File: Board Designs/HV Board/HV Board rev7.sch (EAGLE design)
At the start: 58 parts, among them IC1 OKI-78SR, IC2 NE5532SOIC

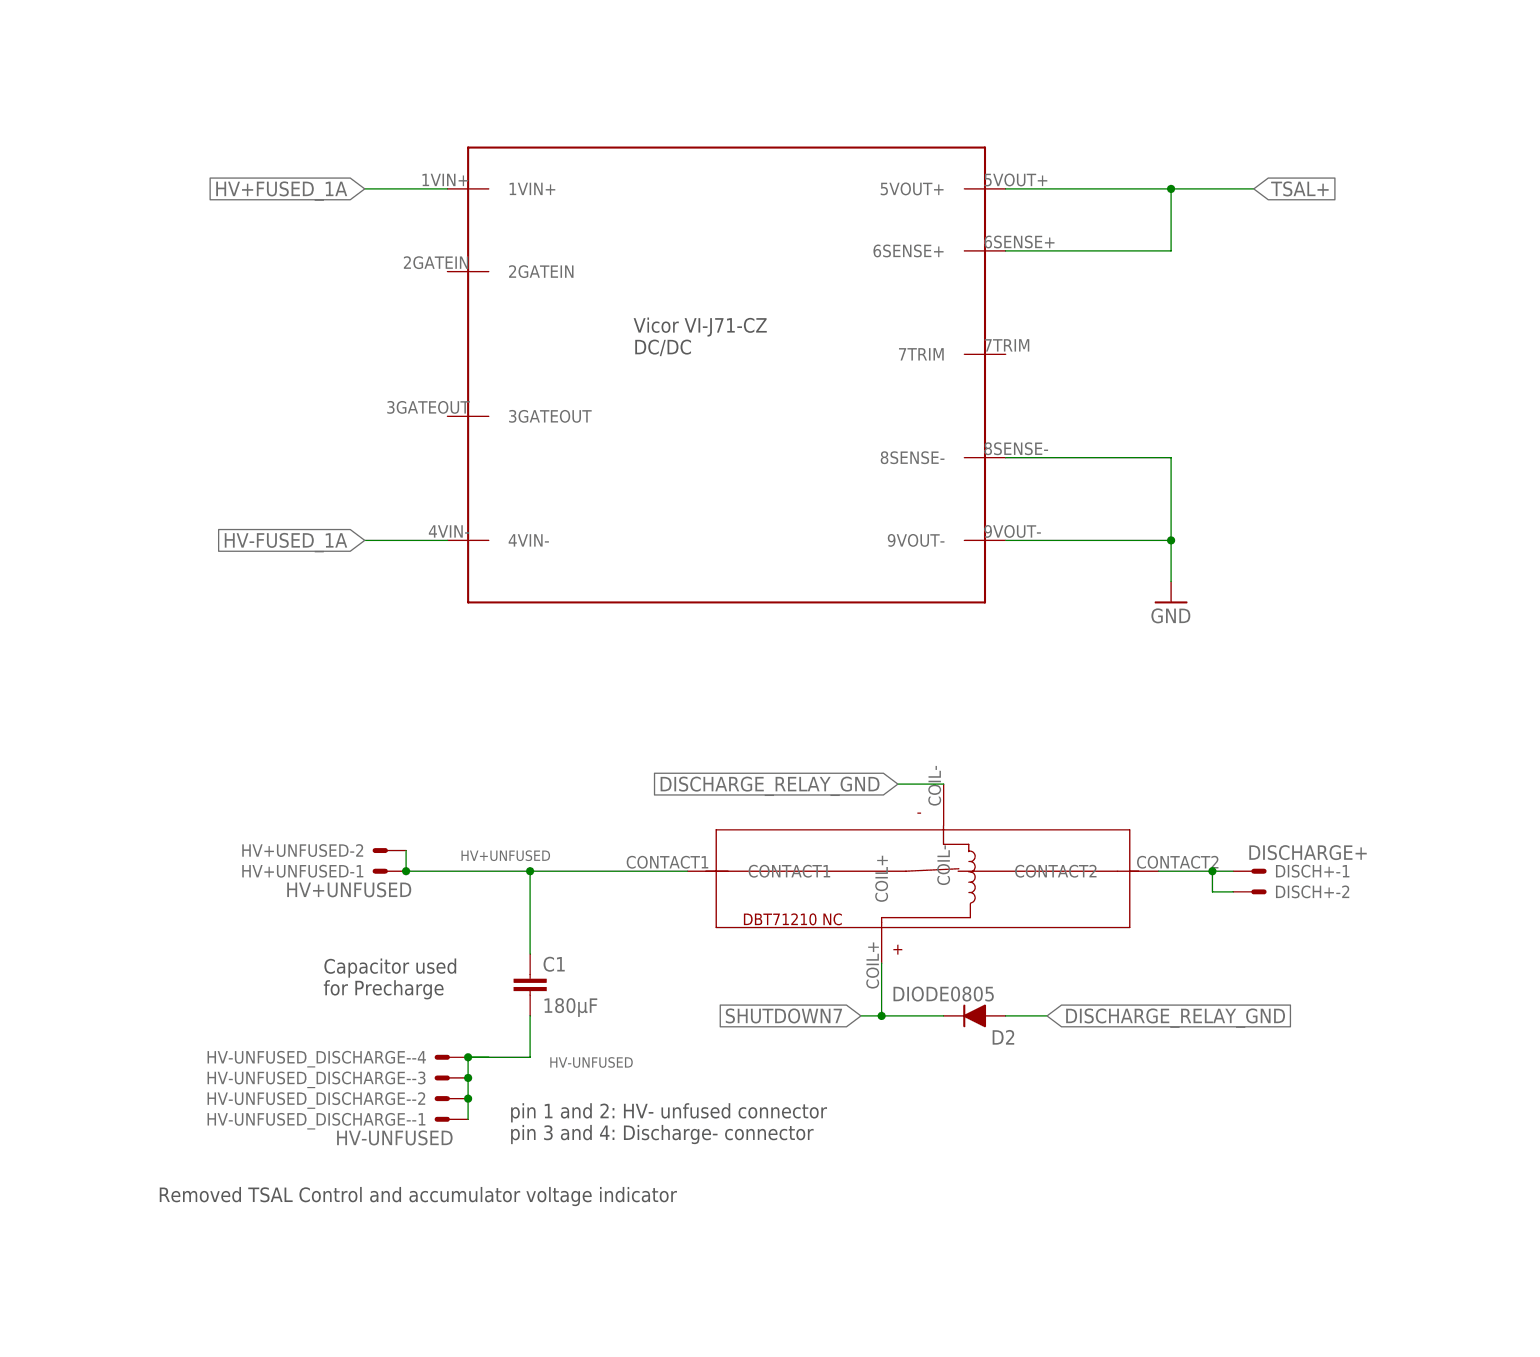
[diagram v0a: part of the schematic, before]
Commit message: Updated cynergy relay in lib, fixed DRC issues
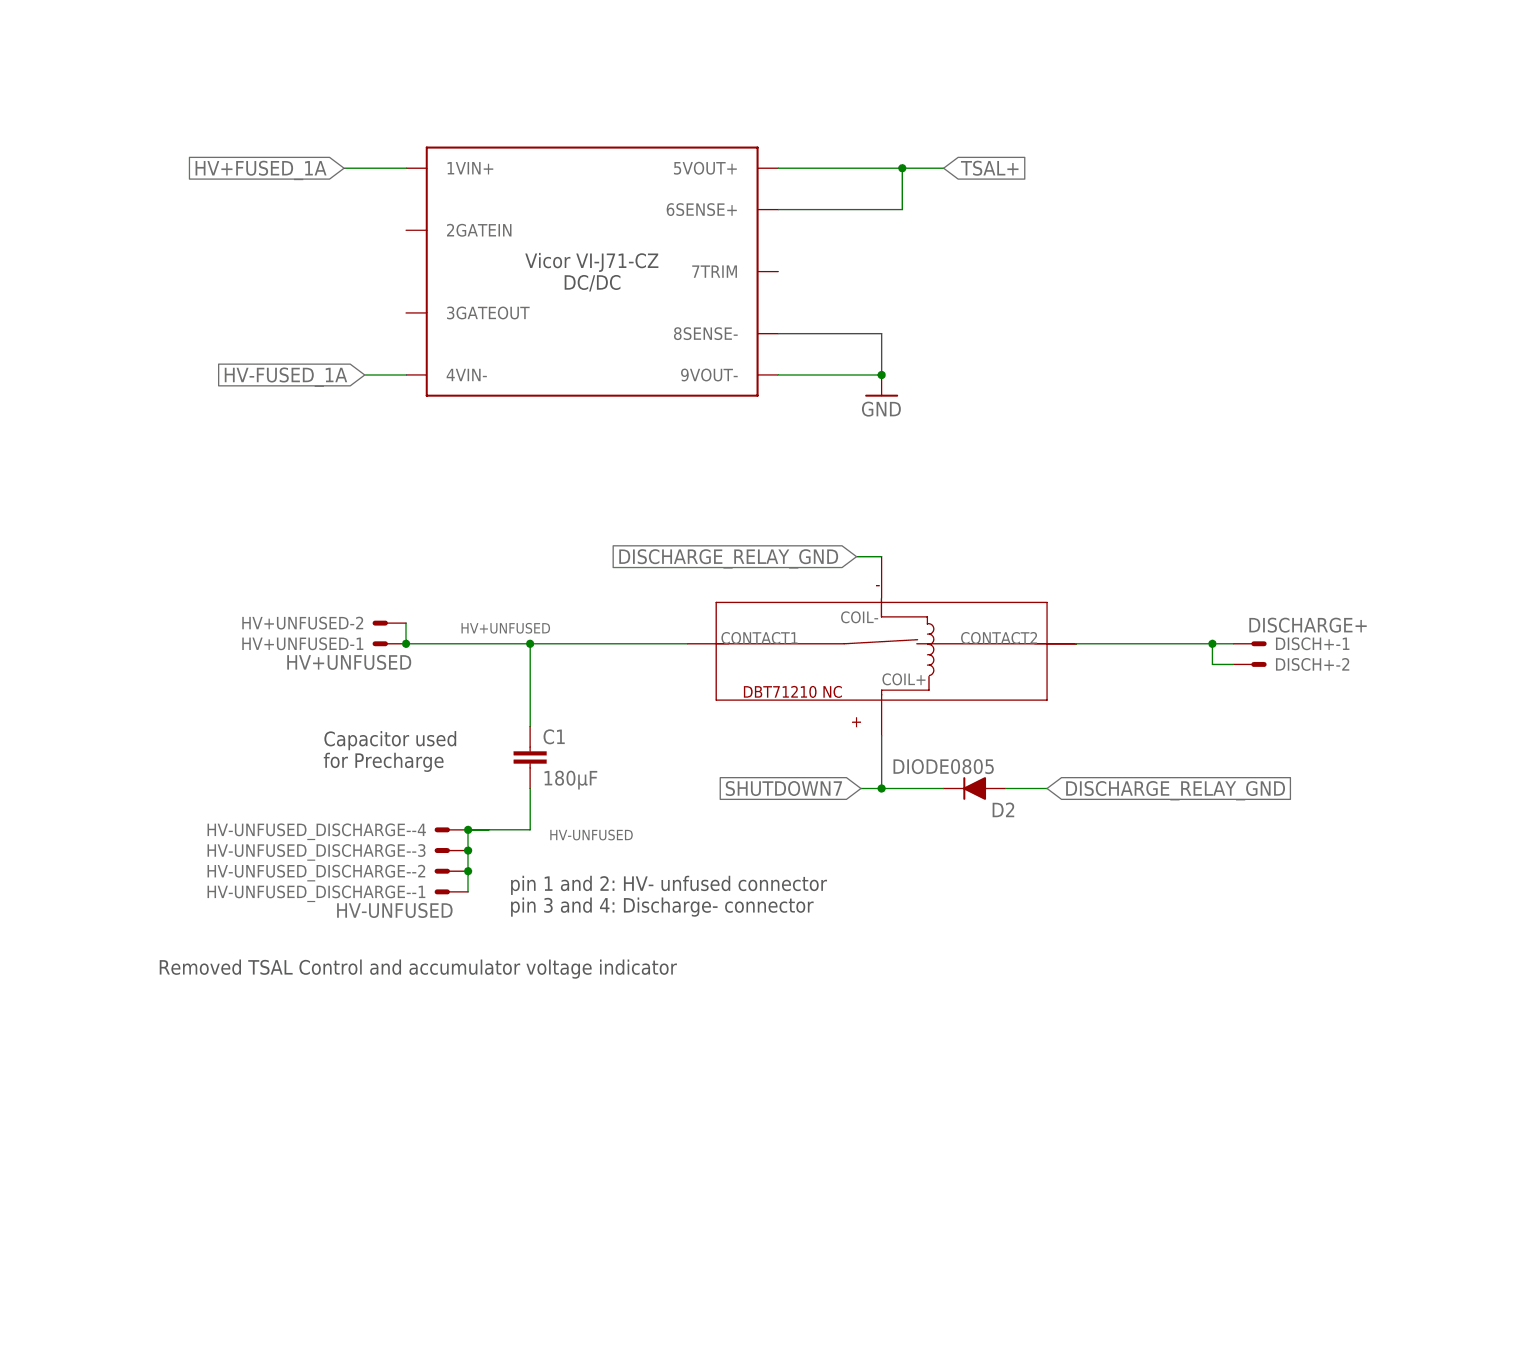
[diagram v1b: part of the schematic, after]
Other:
- moved on the sheet: C1, D2, DISCH+-1, DISCH+-2, HV+UNFUSED-1, HV+UNFUSED-2, HV-UNFUSED_DISCHARGE--1, HV-UNFUSED_DISCHARGE--2, HV-UNFUSED_DISCHARGE--3, HV-UNFUSED_DISCHARGE--4

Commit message: Moved 6820 next to transformer
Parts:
- IMD: value IMD -> CONNECTOR-6NANO-FIT_VERTICAL-6
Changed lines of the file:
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@@
 <part name="MAIN" library="HyTechDevices" deviceset="CONNECTOR-10" device="NANO-FIT_VERTICAL-10" value="MAIN"/>
 <part name="ISO_SPI" library="HyTechDevices" deviceset="CONNECTOR-2" device="NANO-FIT_VERTICAL-2" value="ISO_SPI"/>
-<part name="IMD" library="HyTechDevices" deviceset="CONNECTOR-6" device="NANO-FIT_VERTICAL-6" value="IMD"/>
+<part name="IMD" library="HyTechDevices" deviceset="CONNECTOR-6" device="NANO-FIT_VERTICAL-6" value="CONNECTOR-6NANO-FIT_VERTICAL-6"/>
 <part name="P+6" library="supply1" deviceset="+12V" device=""/>
 <part name="GND17" library="supply1" deviceset="GND" device=""/>

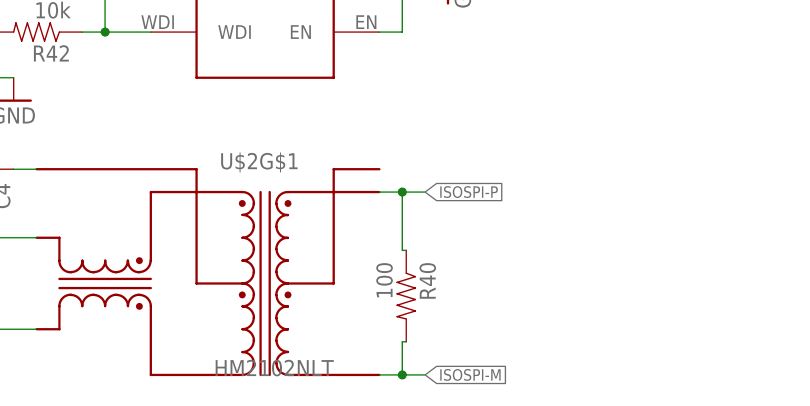
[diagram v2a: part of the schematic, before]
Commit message: Tweak HV board rev{6,7} for manufacturing
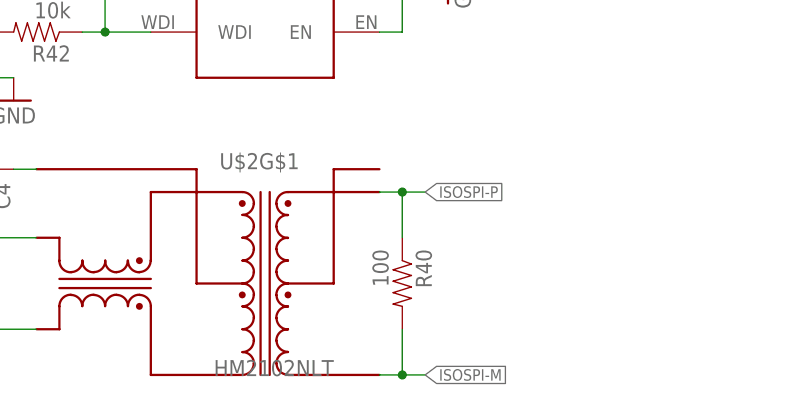
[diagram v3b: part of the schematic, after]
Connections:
- net N$33 renamed IM
- net N$34 renamed IP
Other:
- moved on the sheet: R40
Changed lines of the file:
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@@
 <attribute name="VALUE" x="137.16" y="-251.587" size="1.778" layer="96" rot="MR0"/>
 </instance>
-<instance part="R40" gate="G$1" x="145.22" y="-242.7" smashed="yes" rot="R270">
-<attribute name="NAME" x="146.7186" y="-238.89" size="1.778" layer="95" rot="R270"/>
-<attribute name="VALUE" x="141.918" y="-238.89" size="1.778" layer="96" rot="R270"/>
+<instance part="R40" gate="G$1" x="144.78" y="-241.3" smashed="yes" rot="R270">
+<attribute name="NAME" x="146.2786" y="-237.49" size="1.778" layer="95" rot="R270"/>
+<attribute name="VALUE" x="141.478" y="-237.49" size="1.778" layer="96" rot="R270"/>
 </instance>
 <instance part="C2" gate="G$1" x="109.22" y="-35.56" smashed="yes">
@@
 </segment>
 </net>
-<net name="N$33" class="0">
+<net name="IM" class="0">
 <segment>
 <pinref part="U$8" gate="G$1" pin="IM"/>
@@
 </segment>
 </net>
-<net name="N$34" class="0">
+<net name="IP" class="0">
 <segment>
 <pinref part="U$8" gate="G$1" pin="IP"/>
@@
 <wire x1="144.78" y1="-231.14" x2="142.24" y2="-231.14" width="0.1524" layer="91"/>
 <pinref part="R40" gate="G$1" pin="1"/>
-<wire x1="145.22" y1="-237.62" x2="144.78" y2="-237.62" width="0.1524" layer="91"/>
-<wire x1="144.78" y1="-237.62" x2="144.78" y2="-231.14" width="0.1524" layer="91"/>
+<wire x1="144.78" y1="-236.22" x2="144.78" y2="-231.14" width="0.1524" layer="91"/>
 <junction x="144.78" y="-231.14"/>
 </segment>
@@
 <wire x1="144.78" y1="-251.46" x2="142.24" y2="-251.46" width="0.1524" layer="91"/>
 <pinref part="R40" gate="G$1" pin="2"/>
-<wire x1="145.22" y1="-247.78" x2="144.78" y2="-247.78" width="0.1524" layer="91"/>
-<wire x1="144.78" y1="-247.78" x2="144.78" y2="-251.46" width="0.1524" layer="91"/>
+<wire x1="144.78" y1="-246.38" x2="144.78" y2="-251.46" width="0.1524" layer="91"/>
 <junction x="144.78" y="-251.46"/>
 </segment>

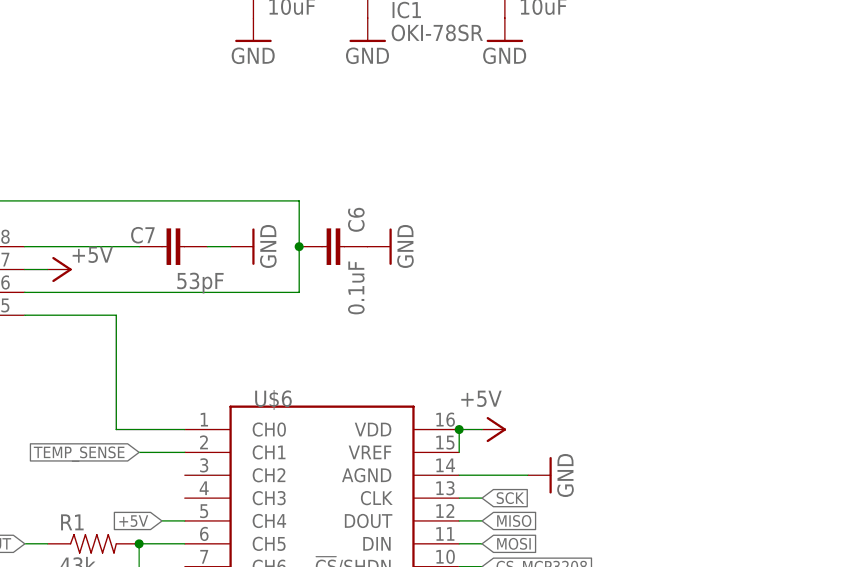
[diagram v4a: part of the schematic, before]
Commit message: HV rev6 & 7: Fixed capacitor value for ADC filter
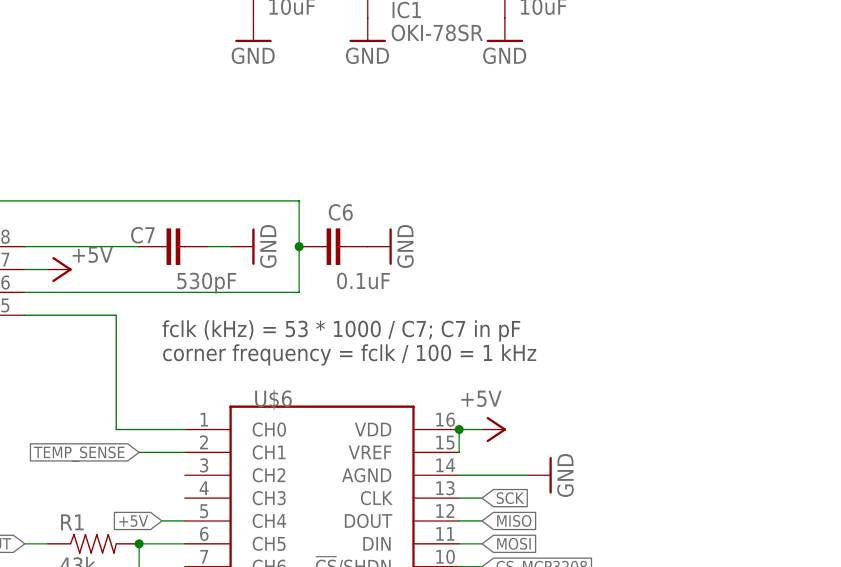
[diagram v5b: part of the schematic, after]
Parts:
- C7: value 53pF -> 530pF
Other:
- note added: "fclk (kHz) = 53 * 1000 / C7; C7 in pF corner frequency = fclk / 100 = 1 kHz"
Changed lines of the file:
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@@
 <part name="C6" library="HyTechDevices" deviceset="CAP" device="0805" value="0.1uF"/>
 <part name="GND10" library="supply1" deviceset="GND" device=""/>
-<part name="C7" library="HyTechDevices" deviceset="CAP" device="0805" value="53pF"/>
+<part name="C7" library="HyTechDevices" deviceset="CAP" device="0805" value="530pF"/>
 <part name="GND14" library="supply1" deviceset="GND" device=""/>
 <part name="MAIN" library="HyTechDevices" deviceset="CONNECTOR-10" device="NANO-FIT_VERTICAL-10" value="MAIN"/>
@@
 <text x="220.98" y="-93.98" size="1.778" layer="97">pin 1 and 2: HV- unfused connector
 pin 3 and 4: Discharge- connector</text>
+<text x="99.06" y="-76.2" size="1.778" layer="97">fclk (kHz) = 53 * 1000 / C7; C7 in pF
+corner frequency = fclk / 100 = 1 kHz</text>
 </plain>
 <instances>
@@
 </instance>
 <instance part="C6" gate="G$1" x="119.38" y="-63.5" smashed="yes" rot="MR270">
-<attribute name="NAME" x="119.761" y="-61.976" size="1.778" layer="95" rot="MR90"/>
-<attribute name="VALUE" x="121.539" y="-65.024" size="1.778" layer="96" rot="MR270"/>
+<attribute name="NAME" x="120.396" y="-60.579" size="1.778" layer="95" rot="MR0"/>
+<attribute name="VALUE" x="118.364" y="-66.421" size="1.778" layer="96" rot="MR180"/>
 </instance>
 <instance part="GND10" gate="1" x="124.46" y="-63.5" smashed="yes" rot="MR270">
